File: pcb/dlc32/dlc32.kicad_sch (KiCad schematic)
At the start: 34 parts, among them IC1 74HCT08, IC2 74HCT04, J1 DOOR1, J12 Conn_01x03, J13 Conn_01x03, J14 Conn_01x03, J2 DOOR2, J3 CHILLER_OK, J7 LASER_AUX, J8 LASER

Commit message: Finalize diagram.
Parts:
- removed J14: Conn_01x03, symbol Connector_Generic:Conn_01x03
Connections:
- net +5V: no longer IC1.1
- new net LASER_EN: IC1.1
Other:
- sheet Serial renamed Sheet2
- sheet Sheet2: file serial.kicad_sch -> sheet2.kicad_sch
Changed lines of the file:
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@@
 	(wire
 		(pts
-			(xy 176.53 71.12) (xy 176.53 82.55)
-		)
-		(stroke
-			(width 0)
-			(type solid)
-		)
-	)
-	(wire
-		(pts
 			(xy 83.82 104.14) (xy 76.2 104.14)
 		)
@@
 	(wire
 		(pts
+			(xy 176.53 68.58) (xy 176.53 82.55)
+		)
+		(stroke
+			(width 0)
+			(type default)
+		)
+	)
+	(wire
+		(pts
 			(xy 48.26 130.81) (xy 48.26 127)
 		)
@@
 	(wire
 		(pts
+			(xy 170.18 68.58) (xy 176.53 68.58)
+		)
+		(stroke
+			(width 0)
+			(type default)
+		)
+	)
+	(wire
+		(pts
 			(xy 172.72 87.63) (xy 181.61 87.63)
 		)
@@
 		)
 	)
+	(global_label "LASER_EN"
+		(shape input)
+		(at 170.18 68.58 180)
+		(fields_autoplaced yes)
+		(effects
+			(font
+				(size 1.524 1.524)
+			)
+			(justify right)
+		)
+		(property "Intersheetrefs" "${INTERSHEET_REFS}"
+			(at 155.4531 68.58 0)
+			(effects
+				(font
+					(size 1.27 1.27)
+				)
+				(justify right)
+				(hide yes)
+			)
+		)
+	)
 	(symbol
 		(lib_id "Device:R")
@@
 	)
 	(symbol
-		(lib_name "74LS08_1")
 		(lib_id "74xx:74LS08")
 		(at 189.23 85.09 0)
@@
 	)
 	(symbol
-		(lib_name "74LS08_2")
 		(lib_id "74xx:74LS08")
 		(at 194.31 105.41 0)
@@
 	)
 	(symbol
-		(lib_id "power:+5V")
-		(at 176.53 71.12 0)
-		(unit 1)
-		(exclude_from_sim no)
-		(in_bom yes)
-		(on_board yes)
-		(dnp no)
-		(property "Reference" "#PWR014"
-			(at 176.53 74.93 0)
-			(effects
-				(font
-					(size 1.27 1.27)
-				)
-				(hide yes)
-			)
-		)
-		(property "Value" "+5V"
-			(at 176.53 67.564 0)
-			(effects
-				(font
-					(size 1.27 1.27)
-				)
-			)
-		)
-		(property "Footprint" ""
-			(at 176.53 71.12 0)
-			(effects
-				(font
-					(size 1.27 1.27)
-				)
-			)
-		)
-		(property "Datasheet" ""
-			(at 176.53 71.12 0)
-			(effects
-				(font
-					(size 1.27 1.27)
-				)
-			)
-		)
-		(property "Description" "Power symbol creates a global label with name \"+5V\""
-			(at 176.53 71.12 0)
-			(effects
-				(font
-					(size 1.27 1.27)
-				)
-				(hide yes)
-			)
-		)
-		(pin "1"
-		)
-		(instances
-			(project ""
-				(path "/fc0b2ef6-7d8e-4322-8468-8fac0c3c3d07"
-					(reference "#PWR014")
-					(unit 1)
-				)
-			)
-		)
-	)
-	(symbol
-		(lib_name "74LS08_3")
 		(lib_id "74xx:74LS08")
 		(at 130.81 115.57 0)
@@
 	)
 	(symbol
-		(lib_id "Connector_Generic:Conn_01x03")
-		(at 96.52 39.37 0)
-		(mirror y)
-		(unit 1)
-		(exclude_from_sim no)
-		(in_bom yes)
-		(on_board yes)
-		(dnp no)
-		(fields_autoplaced yes)
-		(property "Reference" "J14"
-			(at 96.52 30.48 0)
-			(effects
-				(font
-					(size 1.27 1.27)
-				)
-			)
-		)
-		(property "Value" "Conn_01x03"
-			(at 96.52 33.02 0)
-			(effects
-				(font
-					(size 1.27 1.27)
-				)
-			)
-		)
-		(property "Footprint" ""
-			(at 96.52 39.37 0)
-			(effects
-				(font
-					(size 1.27 1.27)
-				)
-				(hide yes)
-			)
-		)
-		(property "Datasheet" "~"
-			(at 96.52 39.37 0)
-			(effects
-				(font
-					(size 1.27 1.27)
-				)
-				(hide yes)
-			)
-		)
-		(property "Description" "Generic connector, single row, 01x03, script generated (kicad-library-utils/schlib/autogen/connector/)"
-			(at 96.52 39.37 0)
-			(effects
-				(font
-					(size 1.27 1.27)
-				)
-				(hide yes)
-			)
-		)
-		(pin "2"
-		)
-		(pin "3"
-		)
-		(pin "1"
-		)
-		(instances
-			(project ""
-				(path "/fc0b2ef6-7d8e-4322-8468-8fac0c3c3d07"
-					(reference "J14")
-					(unit 1)
-				)
-			)
-		)
-	)
-	(symbol
 		(lib_id "Device:R")
 		(at 83.82 109.22 0)
@@
 	)
 	(symbol
-		(lib_name "74LS08_4")
 		(lib_id "74xx:74LS08")
 		(at 157.48 87.63 0)
@@
 			(color 0 0 0 0.0000)
 		)
-		(property "Sheetname" "Serial"
+		(property "Sheetname" "Sheet2"
 			(at 124.46 175.7675 0)
 			(effects
@@
 			)
 		)
-		(property "Sheetfile" "serial.kicad_sch"
+		(property "Sheetfile" "sheet2.kicad_sch"
 			(at 124.46 188.5701 0)
 			(effects

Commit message: Start PCB.
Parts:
- J13: footprint Connector_JST:JST_XH_B3B-XH-A_1x03_P2.50mm_Vertical -> Connector_PinHeader_2.54mm:PinHeader_1x03_P2.54mm_Vertical
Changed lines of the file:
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@@
 			)
 		)
-		(property "Footprint" "Connector_JST:JST_XH_B3B-XH-A_1x03_P2.50mm_Vertical"
+		(property "Footprint" "Connector_PinHeader_2.54mm:PinHeader_1x03_P2.54mm_Vertical"
 			(at 88.9 124.46 0)
 			(effects

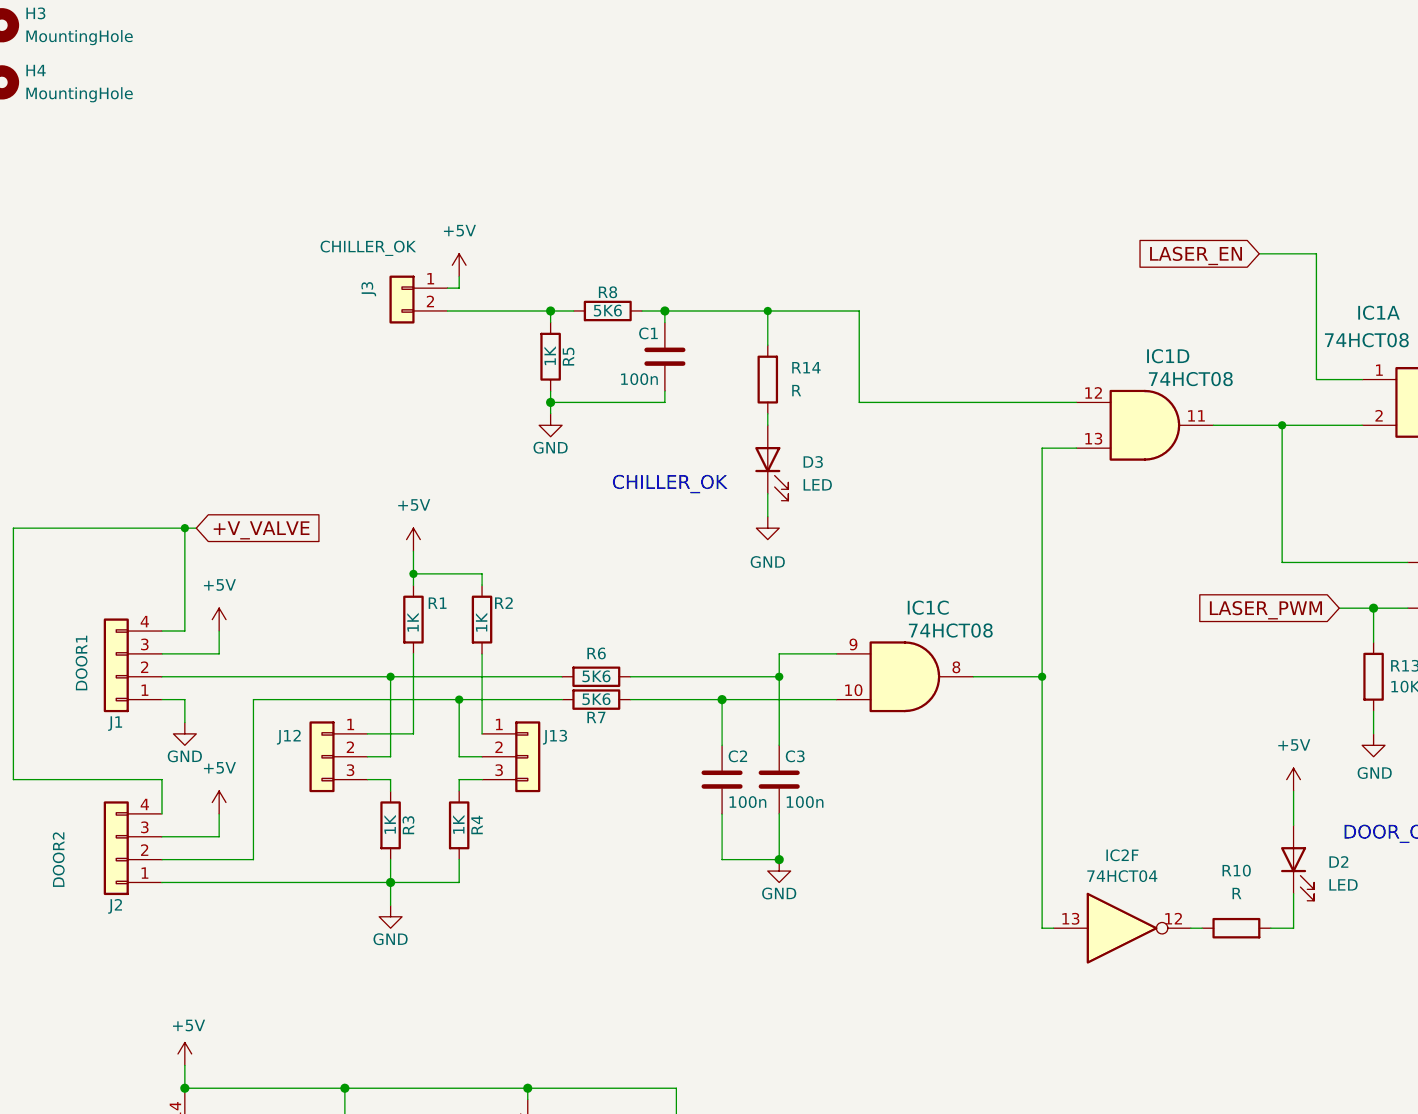
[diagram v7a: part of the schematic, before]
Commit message: Use resistor array.
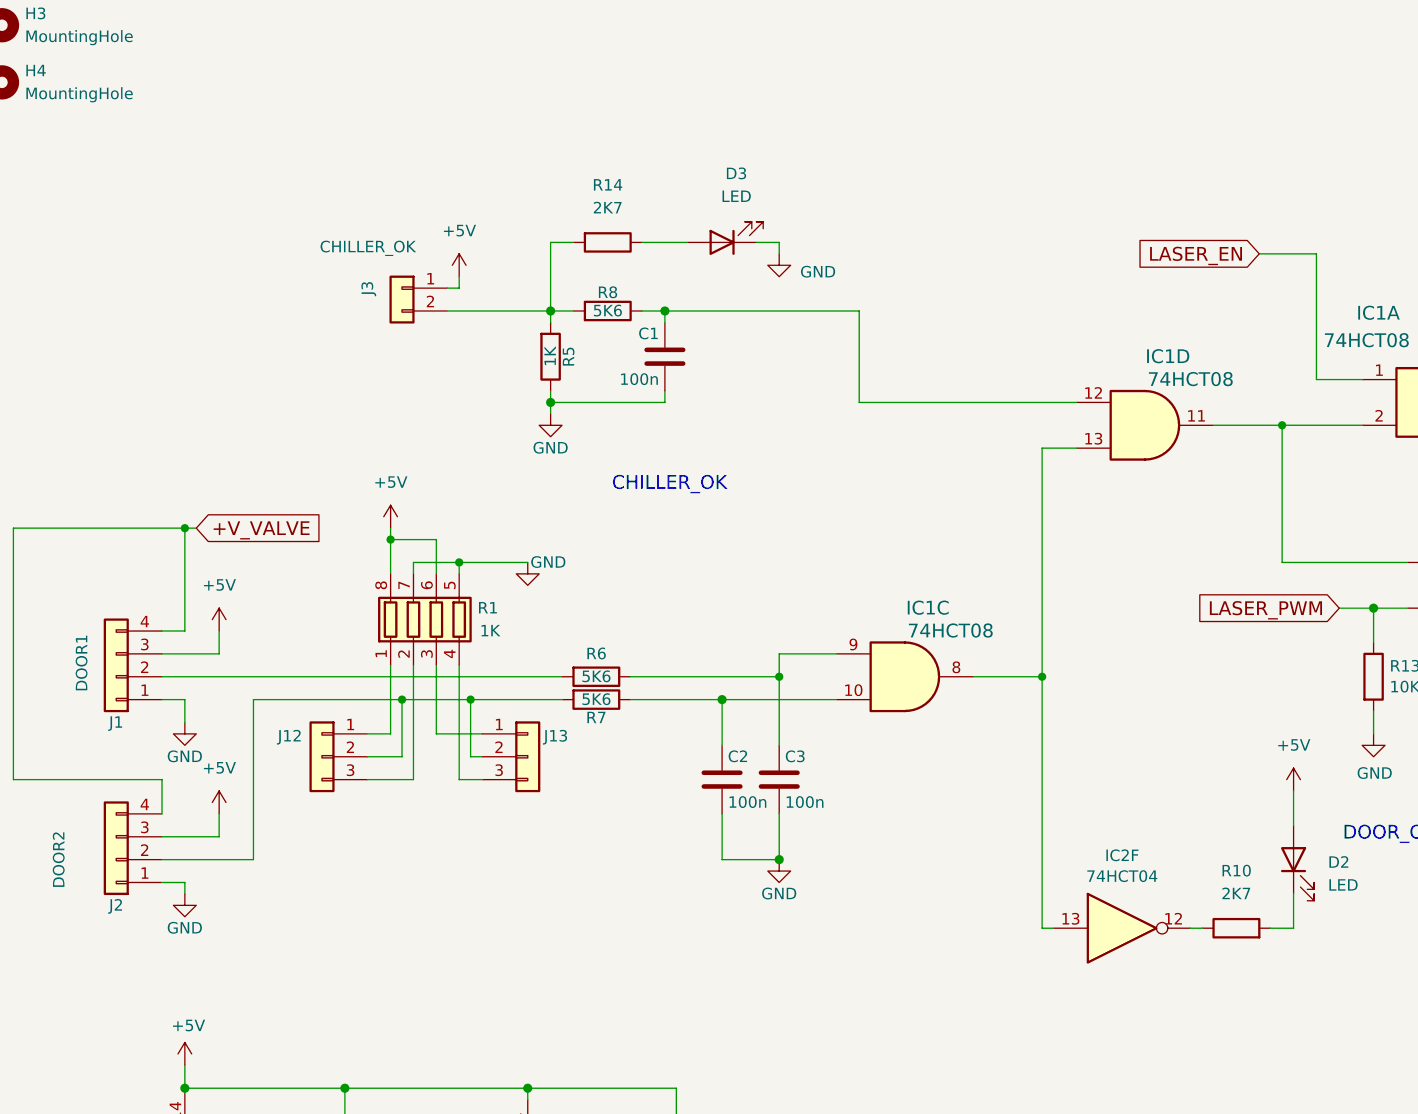
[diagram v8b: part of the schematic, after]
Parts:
- removed R2, R3, R4: 1K, Resistor_SMD:R_0603_1608Metric, symbol Device:R
- C1, C2, C3, C4, C5: footprint Capacitor_SMD:C_0603_1608Metric -> PCM_Capacitor_SMD_AKL:C_0603_1608Metric
- D2, D3, D4: footprint LED_THT:LED_D5.0mm_Horizontal_O1.27mm_Z3.0mm -> PCM_LED_THT_AKL:LED_D5.0mm_Horizontal_O1.27mm_Z3.0mm
- R1: footprint Resistor_SMD:R_0603_1608Metric -> PCM_Resistor_SMD_AKL:R_Array_Concave_4x0603; symbol Device:R -> Device:R_Pack04
- R10, R14: value R -> 2K7; footprint Resistor_SMD:R_0603_1608Metric -> PCM_Resistor_SMD_AKL:R_0603_1608Metric
- R13, R5, R6, R7, R8, R9: footprint Resistor_SMD:R_0603_1608Metric -> PCM_Resistor_SMD_AKL:R_0603_1608Metric
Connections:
- net +5V: now also R1.6 (R3.2), R1.8 (R1.2); no longer R1.1
- net GND: now also R1.5 (R4.2), R1.7 (R2.2)
- net at J12.3 (Pin_3): now also R1.2 (R2.1)
- net at J13.3 (Pin_3): now also R1.4 (R4.1)
- net at J3.2 (Pin_2), R5.2, R8.2: now also R14.2
- net at J1.2 (Pin_2), R6.2: no longer J12.2 (Pin_2)
- net at J13.2 (Pin_2), J2.2 (Pin_2), R7.2: now also J12.2 (Pin_2)
- net at C1.1, IC1.12, R8.1: no longer R14.2
- net at J13.1 (Pin_1): now also R1.3 (R3.1)
- net at J12.1 (Pin_1): now also R1.1 (R1.1); no longer R1.2
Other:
- moved on the sheet: D3, R14
